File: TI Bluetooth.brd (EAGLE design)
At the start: 100 x 80 mm, 43 parts, among them J1 DEBUG Connector, J2 USB Type C Connector, J3 Expansion Header, U1 TPS62160, U2 CC2642R1FRGZRRGZ0048A, Y1 32.768kHz, Y2 48MHz

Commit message: Initial routing
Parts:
- C1: value 10uF -> 1pF
- C10: value 1pF -> 12pF
- C11: value 12pF -> 10uF
- C12: value 1pF -> 22uF
- C13: value 1pF -> 0.1uF
- C15: value 12pF -> 0.1uF
- C16: value 1.8pF -> 22uF
- C2, C5: value 22uF -> 12pF
- C3, C4: value 0.1uF -> 1pF
- C6: value 12pF -> 1.8pF
- D2: value STATUS2 -> STATUS1
- D3: value STATUS1 -> STATUS2
- L2: value 2.2uH -> 6.8nH
- L6: value 6.8nH -> 2.2uH
- R3: value 562k -> 100k
- R4: value 180k -> 56R
- R5, R6: value 100k -> 56R
- R7: value 56R -> 100k
- R8: value 56R -> 562k
- R9: value 56R -> 180k
- U2: value CC2642R1FRGZRRGZ0048A -> CC2642R
- moved D1 194.0 mm to (80.0, 50.8), turned to 180 degrees
- moved D3 189.5 mm to (80.0, 40.6), turned to 180 degrees
- moved D2 186.8 mm to (80.0, 45.7), turned to 180 degrees
- moved R6 175.3 mm to (73.7, 40.6)
- moved R4 174.2 mm to (73.7, 50.8)
- moved R3 173.3 mm to (66.0, 50.8), turned to 180 degrees
- moved C5 160.3 mm to (86.4, 17.8)
- moved R8 155.5 mm to (35.6, 43.2)
- moved C4 153.8 mm to (80.5, 22.9), turned to 90 degrees
- moved R9 149.7 mm to (30.5, 43.2)
- moved C1 149.1 mm to (64.8, 20.3), turned to 90 degrees
- moved L2 140.1 mm to (69.8, 19.6)
- moved C3 139.0 mm to (69.8, 16.0)
- moved U1 137.7 mm to (30.5, 48.3)
- moved C2 136.3 mm to (64.8, 10.2), turned to 270 degrees
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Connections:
- removed net N$4: R1.2, R2.1
- net AGND: now also R1.2, R2.1
- net DCDC_SW_MCU: now also L5.1; no longer L1.1
- net GND: now also C12.2, C15.2, C16.2, C9.1; no longer C3.2, C5.2, C6.1, C9.2, R4.1, R7.1, R8.1
- net JTAG_RESET_MCU: now also R7.1; no longer R5.1
- net N$1: now also C8.2; no longer C7.2
- net N$10: now also L6.1; no longer L2.1
- net N$12: now also C4.1, L3.2, L4.1; no longer C13.1, L5.2, L6.1
- net N$13: now also C3.2, L2.2, L3.1; no longer C12.2, L4.2, L5.1
- net N$14: now also C5.1, L4.2; no longer C15.1, L6.2
- net N$16: now also R8.1, R9.2; no longer R3.1, R4.2
- net N$17: now also C5.2, C6.1; no longer C15.2, C16.1
- net N$18: now also R4.2; no longer R7.2
- net N$19: now also R6.2; no longer R9.2
- net N$2: now also C9.2; no longer C8.2
- net N$20: now also R5.2; no longer R8.2
- net N$24: now also C6.2; no longer C16.2
- net N$3: now also C10.1; no longer C9.1
- net N$6: now also C2.1, L1.2; no longer C11.1, L3.2
- net N$7: now also C7.2; no longer C6.2
- net POWER_LED: now also R3.1, R4.1; no longer D1.A, R6.1
- net RF_N_MCU: now also C1.1, L2.1; no longer C10.1, L4.1
- net RF_P_MCU: now also C3.1, L1.1; no longer C12.1, L3.1
- net STATUS1_LED_MCU: now also R5.1, U2.21; no longer D3.A
- net STATUS2_LED_MCU: now also R6.1, U2.20; no longer D2.A
- net V3P3: now also C16.1, D1.A, D2.A, D3.A, L6.2, R7.2, R8.2; no longer C5.1, L2.2, R5.2, R6.2
- net VBUS_IN: now also C11.1; no longer C1.1
- net VDDR: now also C12.1, C13.1, C15.1, L5.2; no longer C2.1, C3.1, C4.1, L1.2
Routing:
- net STATUS1_LED_MCU: track 0.00 -> 35.2 mm
- net STATUS2_LED_MCU: track 0.00 -> 32.3 mm
- net V3P3: track 0.00 -> 32.0 mm, vias 0 -> 1
- net DIO_1: track 0.00 -> 30.4 mm
- net DIO_3: track 0.00 -> 27.4 mm
- net DIO_2: track 0.00 -> 25.8 mm
- net DIO_5: track 0.00 -> 24.1 mm
- net DIO_4: track 0.00 -> 22.9 mm
- net DIO_7: track 0.00 -> 20.7 mm
- net N$2: track 0.00 -> 20.2 mm, vias 0 -> 2
- net N$1: track 0.00 -> 20.0 mm, vias 0 -> 2
- net DIO_6: track 0.00 -> 19.6 mm
- net DIO_9: track 0.00 -> 19.5 mm
- net DIO_8: track 0.00 -> 17.4 mm
- net DIO_10: track 0.00 -> 15.7 mm
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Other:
- board size 100 x 80 mm -> 101.3 x 76.4 mm

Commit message: More initial routing
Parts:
- moved C15 53.6 mm to (61.0, 12.7), turned to 270 degrees
- moved C14 42.0 mm to (52.1, 35.6), turned to 180 degrees
- moved C12 41.0 mm to (43.2, 17.8), turned to 180 degrees
- moved L5 27.0 mm to (43.2, 22.9), turned to 180 degrees
- moved C13 23.4 mm to (43.2, 12.7), turned to 180 degrees
- moved R7 20.5 mm to (48.3, 20.3), turned to 90 degrees
- moved J2 13.5 mm to (19.1, 24.1)
- moved F1 13.5 mm to (33.0, 30.5)
- moved R1 13.5 mm to (25.4, 31.8)
- moved R2 13.5 mm to (25.4, 26.7)
- moved C11 12.7 mm to (33.0, 41.9)
- moved L6 12.7 mm to (48.3, 40.9)
- moved C16 12.7 mm to (40.6, 47.0)
- moved R9 12.7 mm to (40.6, 35.6)
- moved U1 12.7 mm to (40.6, 40.6)
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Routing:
- net V3P3: track 32.0 -> 91.3 mm, vias 1 -> 4
- net VDDR: track 0.00 -> 34.1 mm, vias 0 -> 3
- net JTAG_TMS_MCU: track 0.00 -> 31.3 mm
- net JTAG_TCK_MCU: track 0.00 -> 28.7 mm
- net JTAG_TDO_MCU: track 0.00 -> 26.9 mm
- net JTAG_TDI_MCU: track 0.00 -> 25.2 mm
- net JTAG_RESET_MCU: track 0.00 -> 19.3 mm, vias 0 -> 2
- net N$5: track 0.00 -> 9.71 mm
- net DCDC_SW_MCU: track 0.00 -> 9.04 mm
- net N$7: track 12.8 -> 16.2 mm
- net N$3: track 12.2 -> 13.1 mm

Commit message: Much of routing finished
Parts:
- moved ANT1 22.4 mm to (86.4, 21.6), turned to 270 degrees
- moved F1 10.5 mm to (22.6, 32.0)
- moved C11 10.3 mm to (22.9, 40.4)
- moved D1 10.2 mm to (69.8, 52.1)
- moved D2 10.2 mm to (69.8, 47.0)
- moved D3 10.2 mm to (69.8, 41.9)
- moved C10 10.2 mm to (45.7, 6.35)
- moved C14 10.2 mm to (41.9, 34.3)
- moved C15 10.2 mm to (50.8, 11.4)
- moved J1 10.2 mm to (25.4, 11.4)
- moved R3 10.2 mm to (55.9, 52.1)
- moved U2 10.2 mm to (45.7, 21.6)
- moved Y2 10.2 mm to (43.2, 11.4)
- moved C16 10.2 mm to (30.5, 45.7)
- moved J2 10.2 mm to (8.89, 25.4)
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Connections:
- removed net N$24: ANT1.FEED, C6.2
- net GND: now also ANT1.FEED, C6.2
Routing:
- net V3P3: track 91.3 -> 159.4 mm, vias 4 -> 8
- net AGND: track 0.00 -> 37.8 mm
- net POWER_LED: track 5.92 -> 37.4 mm, vias 0 -> 2
- net GND: track 0.00 -> 23.0 mm, vias 0 -> 182
- net VBUS: track 0.00 -> 18.9 mm
- net N$16: track 0.00 -> 8.02 mm
- net N$1: track 20.0 -> 19.4 mm
- added copper zone on layer 1, net FEED
- added copper zone on layer 1, net GND
- added copper zone on layer 16, net GND
- added copper zone on layer 1, net N$10
- added copper zone on layer 1, net V3P3
- added copper zone on layer 1, net VBUS_IN
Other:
- board size 101.3 x 76.4 mm -> 99.1 x 61 mm

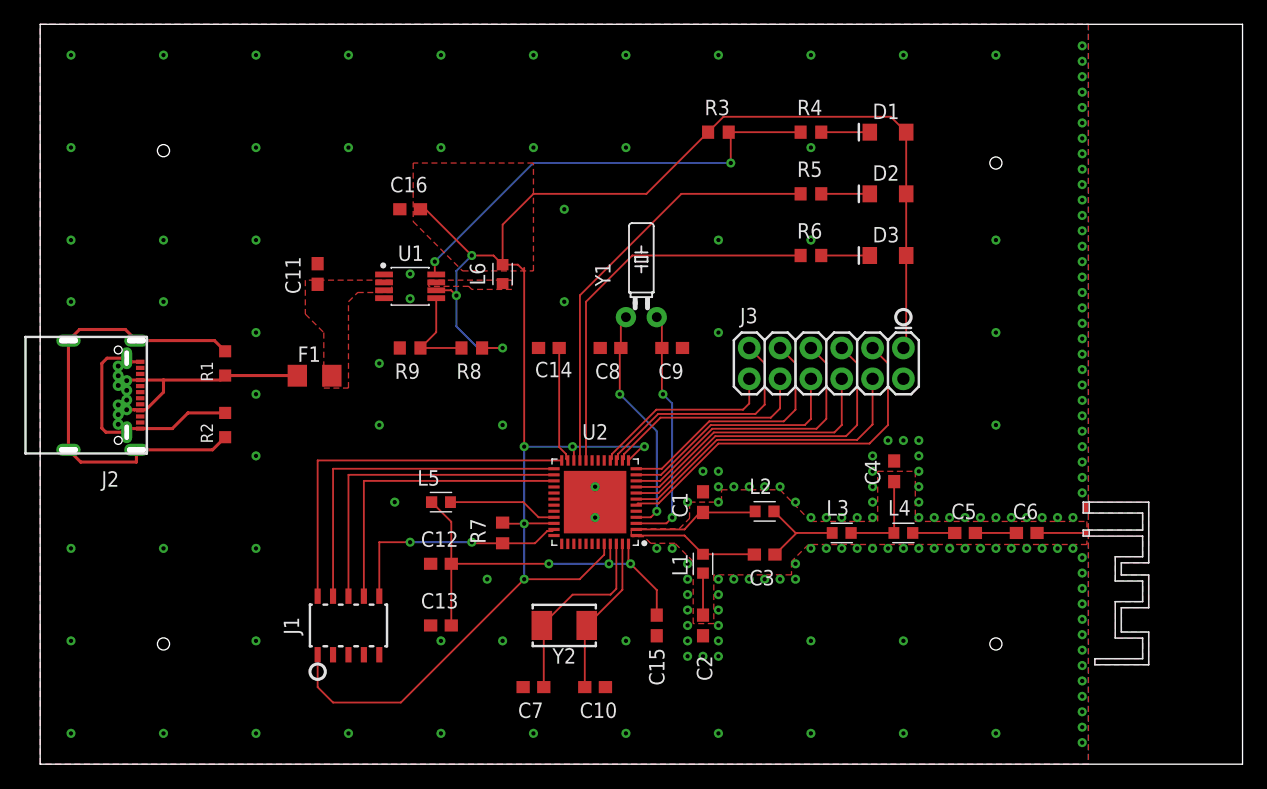
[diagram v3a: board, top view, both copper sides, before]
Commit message: Shrunk board size
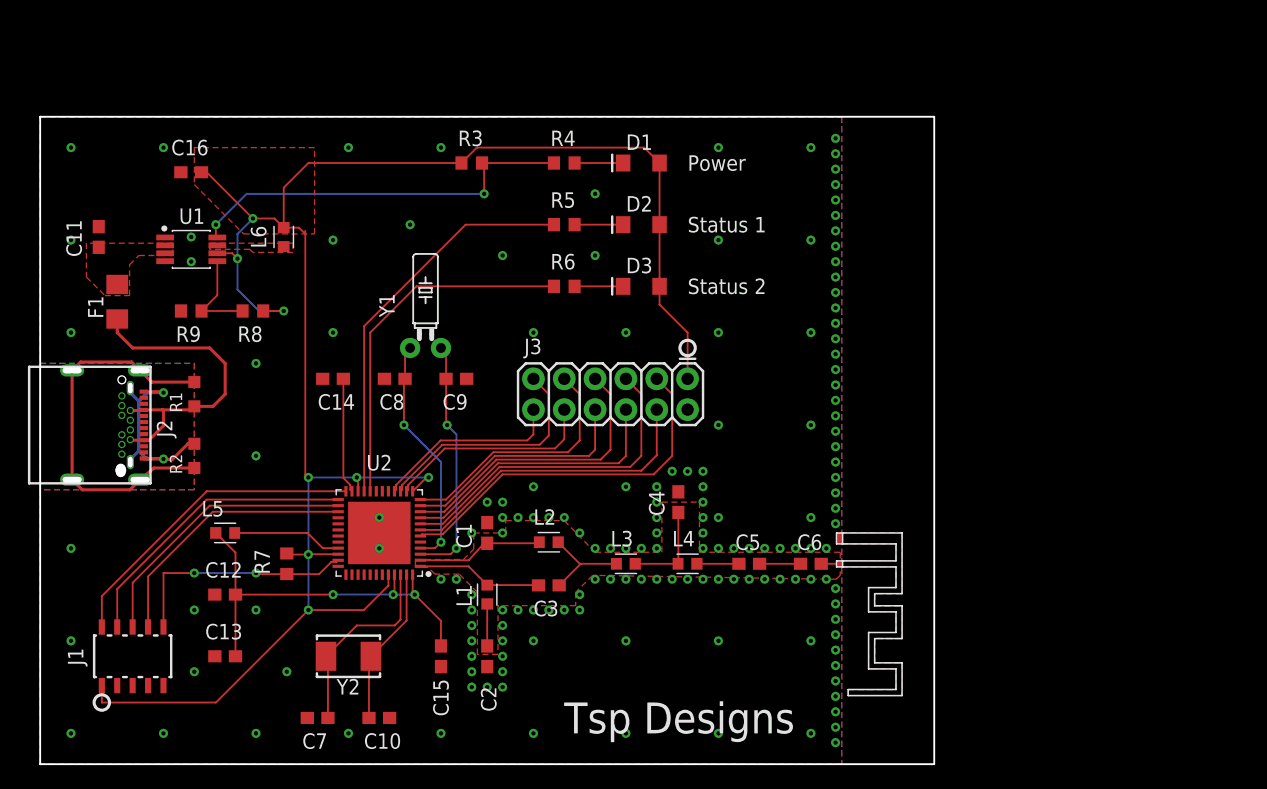
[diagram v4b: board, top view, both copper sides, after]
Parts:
- moved R3 20.5 mm to (35.6, 49.5)
- moved R4 20.5 mm to (43.2, 49.5)
- moved R5 20.5 mm to (43.2, 44.5)
- moved R6 20.5 mm to (43.2, 39.4)
- moved ANT1 20.5 mm to (66.1, 19.1)
- moved D1 20.5 mm to (49.5, 49.5)
- moved D2 20.5 mm to (49.5, 44.5)
- moved D3 20.5 mm to (49.5, 39.4)
- moved L6 18.3 mm to (20.1, 43.4)
- moved R8 18.3 mm to (17.5, 37.3)
- moved C11 18.3 mm to (4.83, 43.4)
- moved C16 18.3 mm to (12.4, 48.8)
- moved R9 18.3 mm to (12.4, 37.3)
- moved U1 18.3 mm to (12.4, 42.4)
- moved L3 18.0 mm to (48.3, 16.5)
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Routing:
- net VBUS: track 18.9 -> 26.5 mm
- net AGND: track 37.8 -> 31.2 mm
- net JTAG_TMS_MCU: track 31.3 -> 26.2 mm
- net POWER_LED: track 37.4 -> 32.8 mm
- net JTAG_TCK_MCU: track 28.7 -> 24.4 mm
- net GND: track 23.0 -> 19.2 mm, vias 182 -> 161
- net JTAG_TDO_MCU: track 26.9 -> 23.2 mm
- net JTAG_TDI_MCU: track 25.2 -> 22.0 mm
- net STATUS2_LED_MCU: track 32.3 -> 29.8 mm
- net STATUS1_LED_MCU: track 35.2 -> 32.7 mm
- net V3P3: track 159.4 -> 158.5 mm
- added copper zone on layer 1, net USB-C
- added copper zone on layer 16, net USB-C
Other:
- board size 99.1 x 61 mm -> 73.7 x 53.3 mm
- board text added: "Power"
- board text added: "Status 1"
- board text added: "Status 2"
- board text added: "Tsp Designs"

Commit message: Fixed PCB antenna and width of power traces
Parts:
- moved C14 4.02 mm to (25.4, 27.9), turned to 90 degrees
- moved ANT1 0.63 mm to (65.5, 19.1)
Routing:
- net N$5: track 9.56 -> 4.68 mm
